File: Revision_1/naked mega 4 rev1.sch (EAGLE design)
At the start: 22 parts, among them IC1 CP2102, J1 USB4105-GF-A

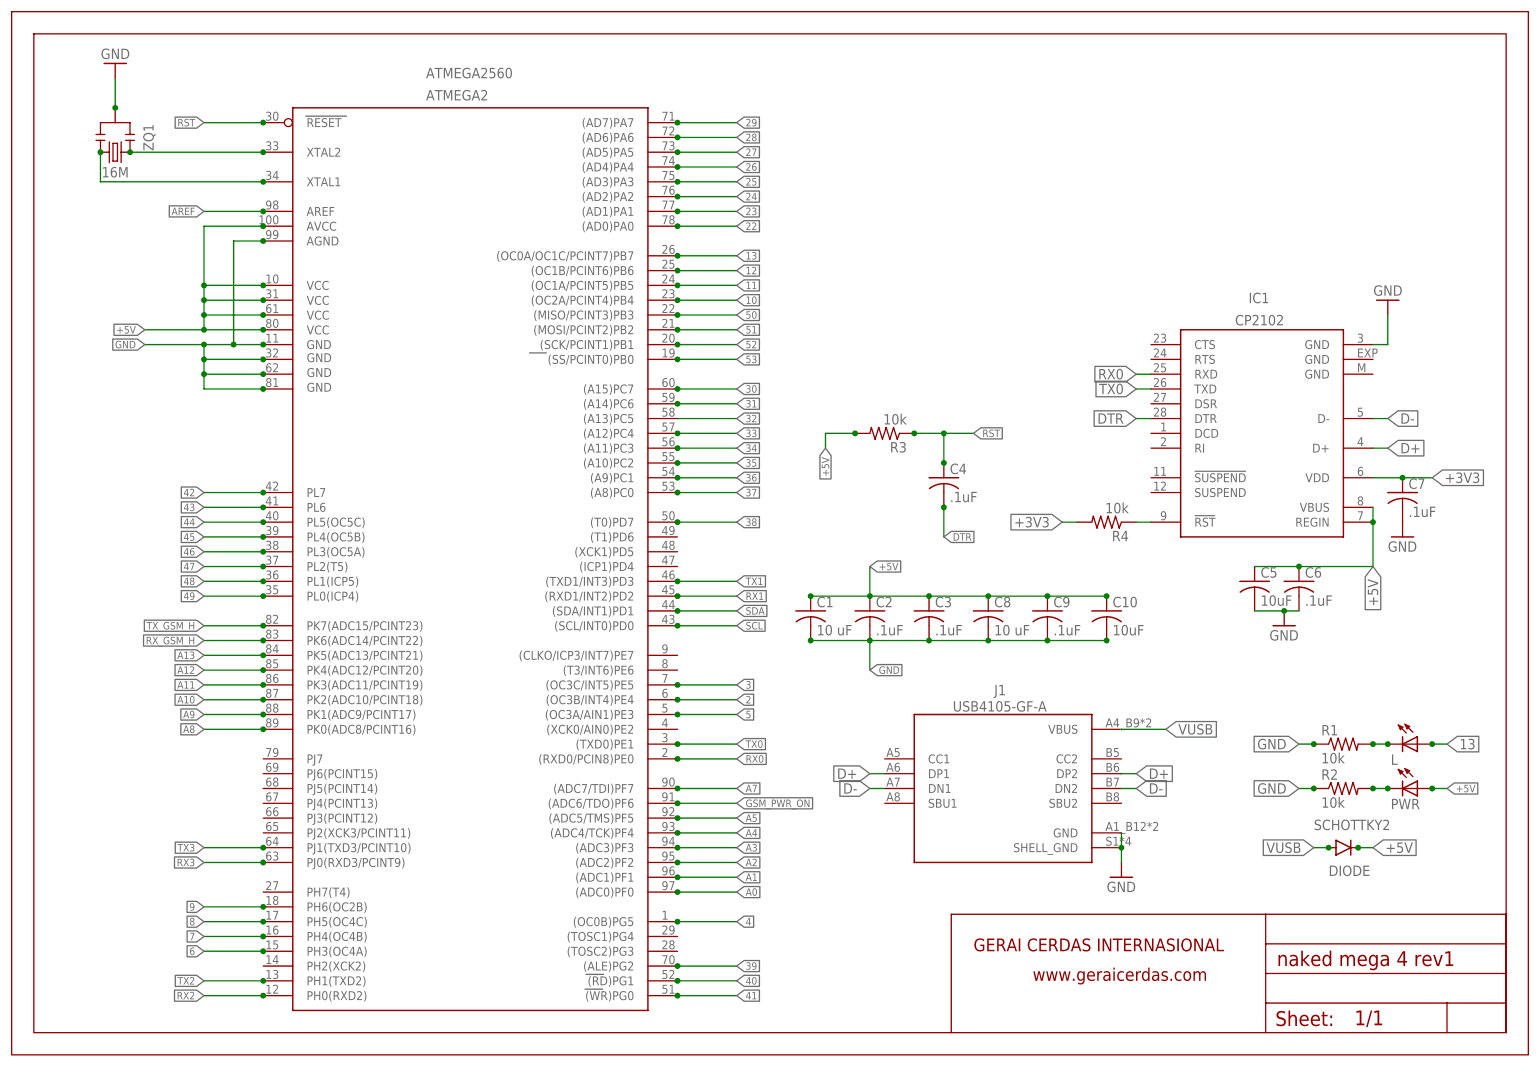
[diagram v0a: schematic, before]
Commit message: fixed wrong tx/rx connection
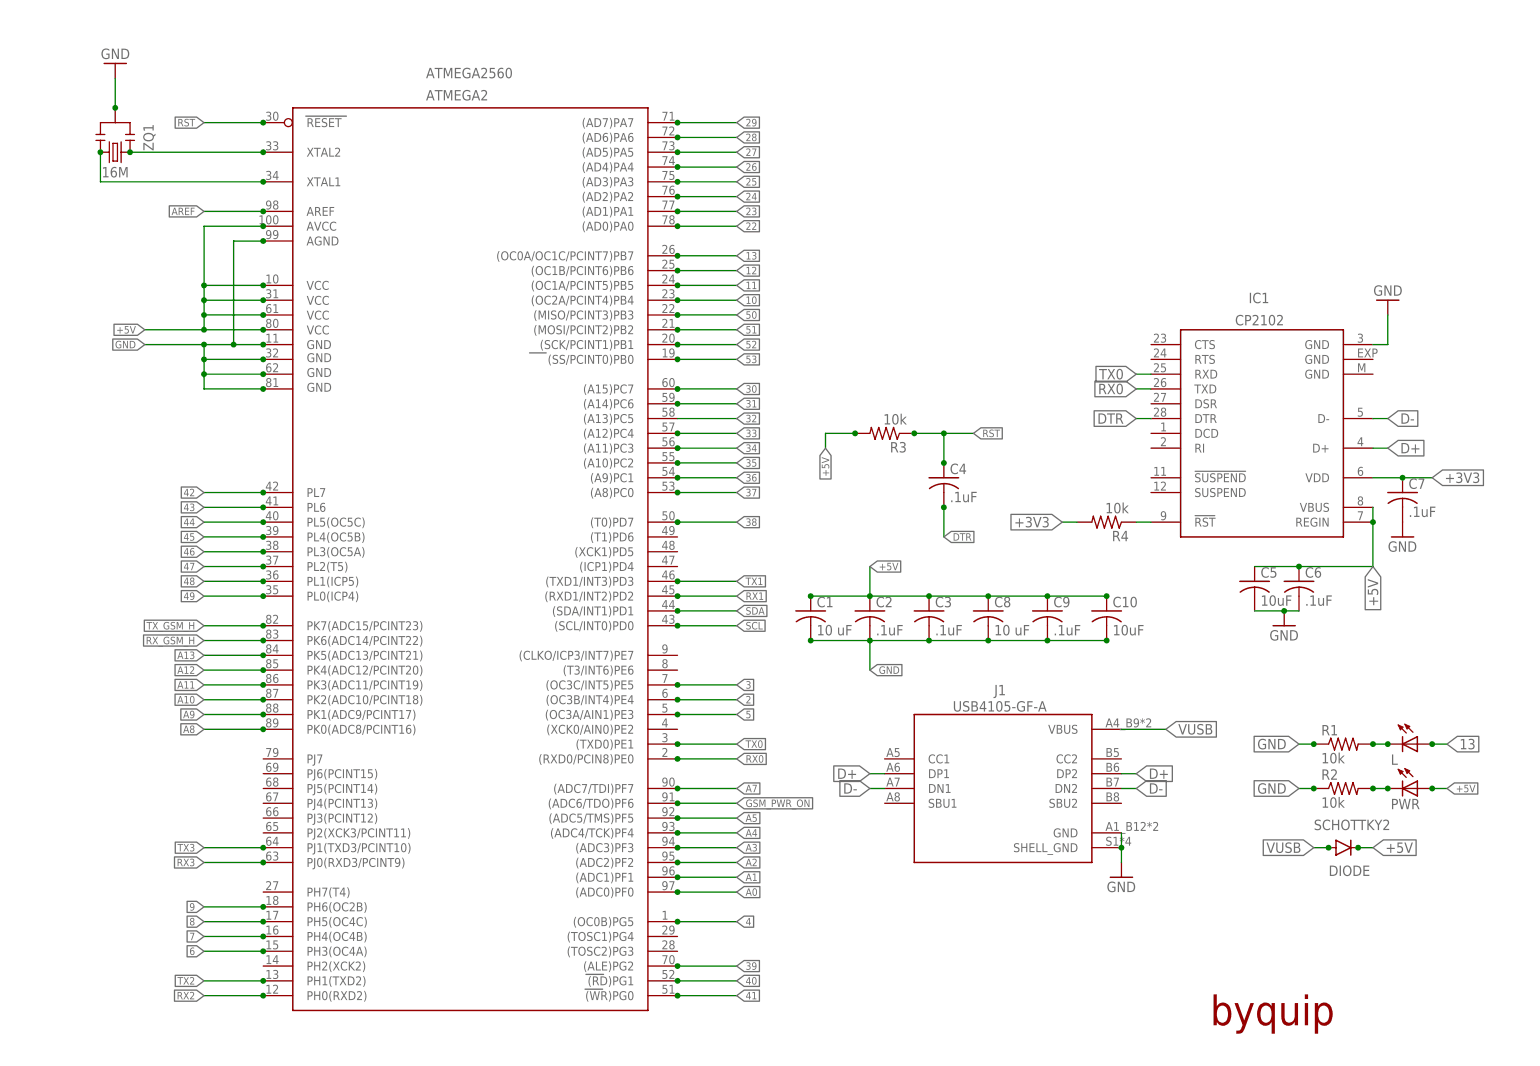
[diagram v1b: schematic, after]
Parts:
- removed U$1: FRAME, geraicerdas:FRAME
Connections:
- net RX0: now also IC1.TXD; no longer IC1.RXD
- net TX0: now also IC1.RXD; no longer IC1.TXD
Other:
- note added: "byquip"
